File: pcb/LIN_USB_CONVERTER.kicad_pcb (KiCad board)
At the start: 2 copper layers, 17.8 x 34 mm, 29 parts, among them J1 Conn_01x03, J2 TerminalBlock, J3 GS2, J4 USB_A, P2 CONN_01X05, U1 TJA1028TK/3V3/20/J, U2 MAX12931BASA+, U3 MCP1700T-3302E/TT, U4 STM32F042G4U6

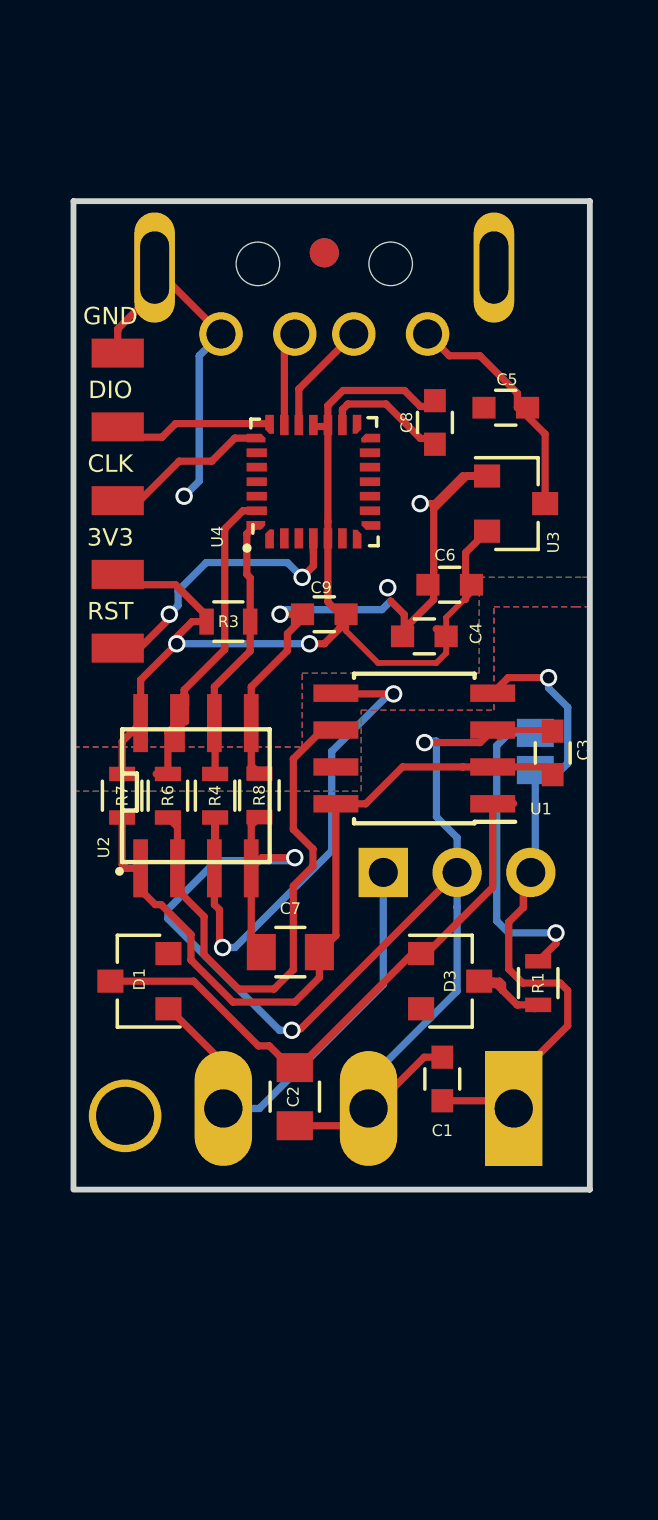
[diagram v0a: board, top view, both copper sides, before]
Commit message: changed to usb-c, tag-connect, and prepared for jlcpcb production
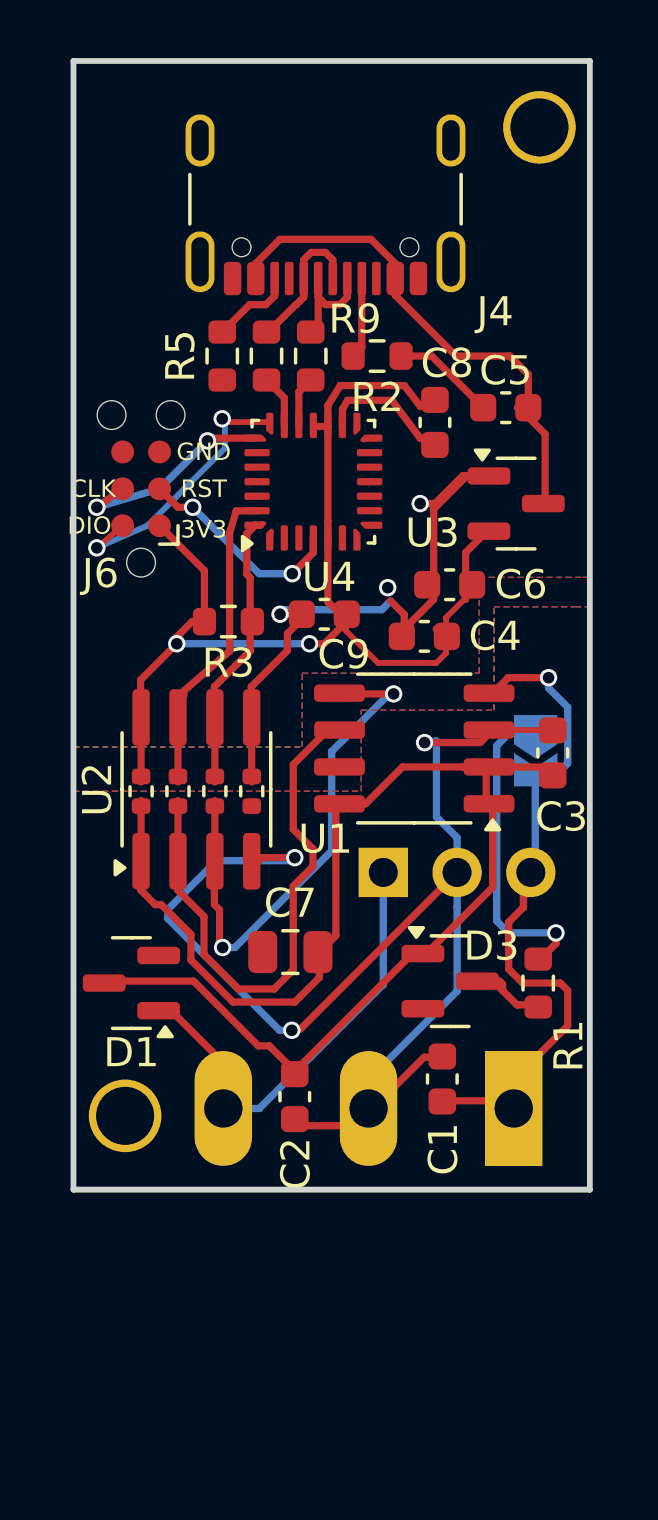
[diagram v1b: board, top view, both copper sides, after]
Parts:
- removed J3: GS2, Connectors:GS2
- removed P2: CONN_01X05, usb_ccb_custom:swd_smd_conn5
- removed f1, f2: fiducial, Fiducials:Fiducial_1mm_Dia_2.54mm_Outer_CopperTop
- added J6: Conn_ARM_SWD_TagConnect_TC2030-NL, Connector:Tag-Connect_TC2030-IDC-NL_2x03_P1.27mm_Vertical, F.Cu at (142.6, 88.2)
- added JP1: Jumper_2_Small_Open, Jumper:SolderJumper-2_P1.3mm_Open_TrianglePad1.0x1.5mm, B.Cu at (156.1, 97.2)
- added R10: 33, Resistor_SMD:R_0603_1608Metric, F.Cu at (146.9, 83.6)
- added R2: 5K1, Resistor_SMD:R_0603_1608Metric, F.Cu at (150.7, 83.6)
- added R5: 5K1, Resistor_SMD:R_0603_1608Metric, F.Cu at (145.3, 83.6)
- added R9: 33, Resistor_SMD:R_0603_1608Metric, F.Cu at (148.4, 83.6)
- added mh2: fiducial, usb_ccb_custom:1pin, F.Cu at (156.3, 75.8)
- C1, C3, C4, C5, C6, C8, C9: footprint Capacitors_SMD:C_0603 -> Capacitor_SMD:C_0603_1608Metric
- C2: footprint Capacitors_SMD:C_0805 -> Capacitor_SMD:C_0603_1608Metric
- C7: footprint Capacitors_SMD:C_0805 -> Capacitor_SMD:C_0805_2012Metric
- D1, D3: value SMBD914E6327HTSA1 -> BAV70; footprint Diodes_SMD:D_SOT-23_ANK -> Package_TO_SOT_SMD:SOT-23
- J1: footprint Pin_Headers:Pin_Header_Straight_1x03_Pitch2.54mm -> Connector_PinHeader_2.54mm:PinHeader_1x03_P2.54mm_Vertical
- J2: footprint Connectors_Terminal_Blocks:TerminalBlock_Altech_AK300-3_P5.00mm -> TerminalBlock:TerminalBlock_Altech_AK300-3_P5.00mm
- J4: value USB_A -> USB_C_Receptacle_USB2.0_16P; footprint usb_ccb_custom:USB_A_DS1097R -> Connector_USB:USB_C_Receptacle_GCT_USB4105-xx-A_16P_TopMnt_Horizontal; moved to F.Cu
- R1, R3: footprint Resistors_SMD:R_0603 -> Resistor_SMD:R_0603_1608Metric
- R4, R6, R7, R8: value 0 -> 0R; footprint Resistors_SMD:R_0603 -> Resistor_SMD:R_0402_1005Metric
- U1: value TJA1028TK/3V3/20/J -> TJA1028T/3V3/20/1J; footprint Housings_SOIC:SOIC-8_3.9x4.9mm_Pitch1.27mm -> Package_SO:SO-8_3.9x4.9mm_P1.27mm
- U2: value MAX12931BASA+ -> ISO7321CDR; footprint usb_ccb_custom:SOIC-8-N_MAXIM -> Package_SO:SOIC-8_3.9x4.9mm_P1.27mm
- U3: value MCP1700T-3302E/TT -> MCP1700T-3302ETT; footprint TO_SOT_Packages_SMD:SOT-23 -> Package_TO_SOT_SMD:SOT-23
- U4: value STM32F042G4U6 -> STM32F042G6U6; footprint usb_ccb_custom:ST_UFQFPN-28_3x3mm_P0.5mm -> Package_DFN_QFN:QFN-28_4x4mm_P0.5mm
- moved J4 6.65 mm to (148.9, 77.3), turned to 180 degrees
- moved R7 0.67 mm to (142.6, 98.6)
- moved R6 0.38 mm to (143.8, 98.6)
- moved R8 0.30 mm to (146.4, 98.6)
- moved D1 0.28 mm to (142.2, 105.2)
- moved U2 0.22 mm to (144.5, 98.6), turned to 90 degrees
- moved R4 0.15 mm to (145.1, 98.6)
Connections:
- C2 pad 1: +BATT -> +3.3VA
- D1 pad 1: +BATT -> Net-(D1-A)
- D1 pad 2: Net-(D1-Pad2) -> (no net)
- D3 pad 1: Net-(D3-Pad1) -> +3.3VA
- D3 pad 2: +BATT -> (no net)
- J1 pad 1: Net-(D1-Pad2) -> Net-(D1-A)
- J2 pad 3: Net-(D1-Pad2) -> Net-(D1-A)
- R1 pad 2: Net-(D3-Pad1) -> Net-(D3-K)
- U1 pad 1: +BATT -> +3.3VA
- U1 pad 7: (no net) -> unconnected-(U1-RSTN-Pad7)
- U4 pad 1: Net-(U4-Pad1) -> unconnected-(U4-PB8-Pad1)
- U4 pad 10: (no net) -> unconnected-(U4-PA4-Pad10)
- U4 pad 11: (no net) -> unconnected-(U4-PA5-Pad11)
- U4 pad 12: (no net) -> unconnected-(U4-PA6-Pad12)
- U4 pad 13: (no net) -> unconnected-(U4-PA7-Pad13)
- U4 pad 14: Net-(U4-Pad14) -> unconnected-(U4-PB0-Pad14)
- U4 pad 15: Net-(U4-Pad15) -> unconnected-(U4-PB1-Pad15)
- U4 pad 2: (no net) -> unconnected-(U4-PF0-Pad2)
- U4 pad 23: (no net) -> unconnected-(U4-PA15-Pad23)
- U4 pad 24: (no net) -> unconnected-(U4-PB3-Pad24)
- U4 pad 25: (no net) -> unconnected-(U4-PB4-Pad25)
- U4 pad 26: (no net) -> unconnected-(U4-PB5-Pad26)
- U4 pad 3: (no net) -> unconnected-(U4-PF1-Pad3)
- U4 pad 6: (no net) -> unconnected-(U4-PA0-Pad6)
- U4 pad 7: Net-(U4-Pad7) -> unconnected-(U4-PA1-Pad7)
- U4 pad 8: Net-(U4-Pad8) -> unconnected-(U4-PA2-Pad8)
- U4 pad 9: (no net) -> unconnected-(U4-PA3-Pad9)
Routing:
- net +3.3VA: track 27.9 -> 49.1 mm
- net +BATT: track 20.3 -> 0.00 mm
- net Net-(D1-Pad2): track 18.4 -> 0.00 mm
- net Net-(D1-A): track 0.00 -> 18.4 mm
- net +5V: track 8.16 -> 17.7 mm
- net GND: track 39.7 -> 30.7 mm, vias 4 -> 3
- net Net-(J4-D+-PadA6): track 0.00 -> 4.92 mm
- net -BATT: track 52.3 -> 47.6 mm
- net Net-(J4-D--PadA7): track 0.00 -> 4.45 mm
- net SW_DIO: track 5.79 -> 9.93 mm, vias 0 -> 2
- net Net-(D3-Pad1): track 3.79 -> 0.00 mm
- net Net-(D3-K): track 0.00 -> 3.79 mm
- net Net-(J4-CC2): track 0.00 -> 2.92 mm
- net Net-(J4-CC1): track 0.00 -> 2.79 mm
- net Net-(J6-~{RESET}): track 10.4 -> 7.84 mm
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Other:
- board size 17.8 x 34 mm -> 17.8 x 38.9 mm
- net class Default removed
- net class Motor removed

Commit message: moved terminals to top, added mounting holes
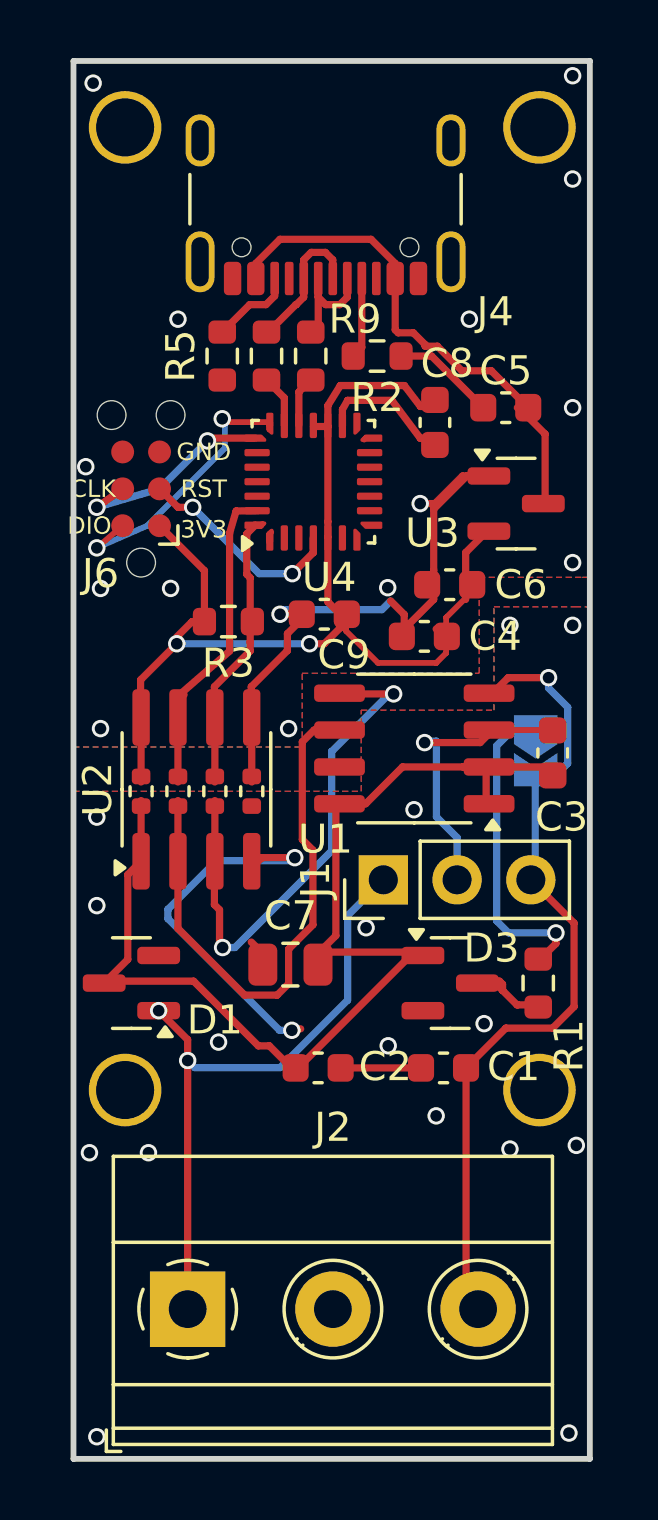
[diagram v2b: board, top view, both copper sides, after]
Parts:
- added mh3: fiducial, usb_ccb_custom:1pin, F.Cu at (142.0, 75.8)
- added mh4: fiducial, usb_ccb_custom:1pin, F.Cu at (156.3, 75.8)
- J1: moved to F.Cu
- J2: footprint TerminalBlock:TerminalBlock_Altech_AK300-3_P5.00mm -> TerminalBlock_Phoenix:TerminalBlock_Phoenix_MKDS-1,5-3_1x03_P5.00mm_Horizontal; moved to F.Cu
- moved mh2 33.1 mm to (156.3, 108.9)
- moved J2 13.2 mm to (144.2, 116.5), turned to 0 degrees
- moved C2 1.28 mm to (148.6, 108.1), turned to 0 degrees
- moved mh1 0.89 mm to (142.0, 108.9)
- moved C7 0.43 mm to (147.7, 104.6)
- moved C1 0.38 mm to (153.0, 108.1), turned to 180 degrees
- moved J1 0.25 mm to (150.9, 101.7), turned to 90 degrees
- moved D3 0.07 mm to (153.2, 105.2)
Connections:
- J2 pad 1: Net-(J1-Pin_3) -> Net-(D1-A)
- J2 pad 3: Net-(D1-A) -> Net-(J1-Pin_3)
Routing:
- net -BATT: track 47.6 -> 26.4 mm, vias 3 -> 19
- net +3.3VA: track 49.1 -> 40.6 mm
- net Net-(D1-A): track 18.4 -> 22.6 mm, vias 0 -> 2
- net Net-(J1-Pin_3): track 24.8 -> 28.5 mm
- net Net-(U1-TXD): track 18.1 -> 19.6 mm
- net GND: vias 3 -> 15
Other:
- board size 17.8 x 38.9 mm -> 17.8 x 48.1 mm

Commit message: final production check, moved vias
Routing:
- net GND: track 30.7 -> 22.9 mm
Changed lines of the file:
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@@
 		(tags "capacitor")
 		(property "Reference" "C1"
-			(at -2.413 0.042 360)
+			(at -2.413 0.042 0)
 			(layer "F.SilkS")
 			(effects
@@
 		)
 		(property "Value" "220p"
-			(at 0 1.43 360)
+			(at 0 1.43 0)
 			(layer "F.Fab")
 			(effects
@@
 		)
 		(fp_text user "${REFERENCE}"
-			(at 0 0 360)
+			(at 0 0 0)
 			(layer "F.Fab")
 			(effects
@@
 		)
 		(fp_text user "${REFERENCE}"
-			(at 0 2.54 360)
+			(at 0 2.54 0)
 			(layer "F.Fab")
 			(effects
@@
 	)
 	(segment
-		(start 152.668 88.718)
-		(end 152.16 88.718)
-		(width 0.25)
-		(layer "F.Cu")
-		(net 1)
-	)
-	(segment
 		(start 146.3434 95.0264)
 		(end 147.588 93.7818)
@@
 	)
 	(segment
-		(start 153.618 87.768)
-		(end 152.668 88.718)
-		(width 0.25)
-		(layer "F.Cu")
-		(net 1)
-	)
-	(segment
 		(start 148.258 92.528)
 		(end 147.588 93.198)
@@
 	)
 	(segment
-		(start 151.61 92.536)
-		(end 151.144 92.07)
-		(width 0.25)
-		(layer "F.Cu")
-		(net 1)
-	)
-	(segment
 		(start 152.168 86.474)
 		(end 151.186 85.162)
@@
 	)
 	(segment
-		(start 151.61 93.036)
-		(end 151.61 92.536)
-		(width 0.25)
-		(layer "F.Cu")
-		(net 1)
-	)
-	(segment
 		(start 152.626 91.012)
 		(end 152.626 91.512)
@@
 	)
 	(segment
-		(start 154.462 87.768)
-		(end 153.618 87.768)
-		(width 0.25)
-		(layer "F.Cu")
-		(net 1)
-	)
-	(segment
 		(start 152.626 91.512)
 		(end 152.626 92.02)
@@
 	)
 	(via
-		(at 147.63 96.465)
+		(at 147.63 95.957)
 		(size 0.6)
 		(drill 0.4)
@@
 	)
 	(segment
-		(start 150.844001 92.369999)
-		(end 147.492001 92.369999)
-		(width 0.25)
-		(layer "B.Cu")
-		(net 1)
-	)
-	(segment
-		(start 147.492001 92.369999)
-		(end 147.334 92.528)
-		(width 0.25)
-		(layer "B.Cu")
-		(net 1)
-	)
-	(segment
-		(start 151.144 92.07)
-		(end 150.844001 92.369999)
-		(width 0.25)
-		(layer "B.Cu")
-		(net 1)
-	)
-	(segment
 		(start 153.0536 93.865)
 		(end 152.7142 94.2044)
@@
 	)
 	(segment
-		(start 152.3124 96.9476)
-		(end 154.225 96.9476)
+		(start 152.3632 96.5158)
+		(end 154.6568 96.5158)
 		(width 0.25)
 		(layer "F.Cu")
@@
 	)
 	(segment
-		(start 152.189 108.149)
-		(end 149.421 108.149)
+		(start 152.3124 96.465)
+		(end 152.3632 96.5158)
 		(width 0.25)
 		(layer "F.Cu")
@@
 	)
 	(segment
-		(start 146.7098 100.91)
-		(end 146.3434 101.2764)
+		(start 152.189 108.149)
+		(end 149.421 108.149)
 		(width 0.25)
 		(layer "F.Cu")
@@
 	)
 	(segment
-		(start 154.225 96.9476)
-		(end 154.6568 96.5158)
+		(start 146.7098 100.91)
+		(end 146.3434 101.2764)
 		(width 0.25)
 		(layer "F.Cu")
@@
 	)
 	(via
-		(at 152.3124 96.9476)
+		(at 152.3124 96.465)
 		(size 0.6)
 		(drill 0.4)
@@
 	)
 	(via
-		(at 142.804 111.07)
+		(at 143.058 110.943)
 		(size 0.6)
 		(drill 0.4)
@@
 	)
 	(via
-		(at 155.25 110.943)
+		(at 154.869 110.816)
 		(size 0.6)
 		(drill 0.4)
@@
 	)
 	(via
-		(at 141.026 99.513)
+		(at 141.026 99.259)
 		(size 0.6)
 		(drill 0.4)
@@
 	)
 	(via
-		(at 141.026 102.561)
+		(at 140.899 103.831)
 		(size 0.6)
 		(drill 0.4)
@@
 	)
 	(via
-		(at 154.361 106.625)
+		(at 153.98 106.498)
 		(size 0.6)
 		(drill 0.4)
@@
 	)
 	(via
-		(at 152.71 109.8)
+		(at 152.583 109.673)
 		(size 0.6)
 		(drill 0.4)
@@
 	)
 	(via
-		(at 151.059 107.387)
+		(at 150.805 107.133)
 		(size 0.6)
 		(drill 0.4)
@@
 	)
 	(segment
-		(start 152.7188 99.504719)
-		(end 152.7188 96.8968)
-		(width 0.25)
-		(layer "B.Cu")
-		(net 9)
-	)
-	(segment
-		(start 147.7404 101.0116)
-		(end 147.842 100.91)
+		(start 152.7188 96.8714)
+		(end 152.7188 99.504719)
 		(width 0.25)
 		(layer "B.Cu")
@@
 	)
 	(segment
-		(start 145.1496 101.0116)
-		(end 147.7404 101.0116)
+		(start 152.3124 96.465)
+		(end 152.7188 96.8714)
 		(width 0.25)
 		(layer "B.Cu")
@@
 	)
 	(segment
-		(start 153.43 101.418)
-		(end 153.43 100.215919)
+		(start 147.7404 101.0116)
+		(end 147.842 100.91)
 		(width 0.25)
 		(layer "B.Cu")
@@
 	)
 	(segment
-		(start 152.3632 96.8968)
-		(end 152.3124 96.9476)
+		(start 145.1496 101.0116)
+		(end 147.7404 101.0116)
 		(width 0.25)
 		(layer "B.Cu")
@@
 	(segment
 		(start 153.43 100.215919)
-		(end 152.7188 99.504719)
+		(end 153.43 101.418)
 		(width 0.25)
 		(layer "B.Cu")
@@
 	)
 	(segment
-		(start 152.7188 96.8968)
-		(end 152.3632 96.8968)
+		(start 147.316136 106.8536)
+		(end 143.4732 103.010664)
 		(width 0.25)
 		(layer "B.Cu")
@@
 	)
 	(segment
-		(start 147.316136 106.8536)
-		(end 143.4732 103.010664)
+		(start 152.7188 99.504719)
+		(end 153.43 100.215919)
 		(width 0.25)
 		(layer "B.Cu")
